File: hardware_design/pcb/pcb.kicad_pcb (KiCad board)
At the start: 2 copper layers, 117.2 x 110 mm, 98 parts, among them J1 Eurorack Power, J10 Conn_01x10_Socket, J11 Conn_01x10_Socket, J12 Conn_01x10_Pin, J13 Conn_01x10_Socket, J14 Conn_01x10_Pin, J15 Conn_01x10_Socket, J16 Conn_01x10_Pin, J2 Thonkiconn, J3 Thonkiconn, J4 Thonkiconn, J5 Thonkiconn, J6 Thonkiconn, J7 Thonkiconn, J9 Conn_01x10_Pin, Q1 DMG2305UX, Q2 MMBT3904, Q3 MMBT3904, SW1 SW_Rotary_1x4, SW2 SW_SPST, SW3 RotaryEncoder_Switch, SW4 SW_SPST, SW5 SW_Rotary_1x8, U1 Pico, U2 PCM1808, U3 TL072CD, U4 TL072CD, U5 GY_PCM5102A, U6 APS6404L, U7 LM1117MP-5.0, U8 MC14532B

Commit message: Rev 2 schematic & circuit board
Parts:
- removed C18, C19: 22u, Capacitor_SMD_AKL:CP_Elec_6.3x5.8
- removed C20: 100n, Capacitor_SMD_AKL:C_0603_1608Metric
- removed D3, D4, D5, D6: 1N4148WS, Diode_SMD_AKL:D_SOD-323
- removed the G*** at (123.7, 103.7)
- removed the G*** at (59.0, 34.3)
- removed the G*** at (59.7, 34.3)
- removed the G*** at (117.8, 81.4)
- removed R20: 4k7, Resistor_SMD_AKL:R_0603_1608Metric_Pad1.05x0.95mm_HandSolder
- removed R21: 3k3, Resistor_SMD_AKL:R_0603_1608Metric_Pad1.05x0.95mm_HandSolder
- removed R22: 10k, Resistor_SMD_AKL:R_0603_1608Metric_Pad1.05x0.95mm_HandSolder
- removed the REF** at (138.6, 36.4)
- removed the REF** at (59.2, 43.5) (x2)
- removed the REF** at (118.1, 89.9)
- added G***: LOGO, europi:AM_Logo, F.Cu at (117.0, 66.5)
- added G***: LOGO, europi:AM_Logo, F.Cu at (59.7, 35.8)
- added G***: LOGO, europi:AM_Logo, B.Cu at (58.1, 35.5)
- added G***: LOGO, europi:AM_Logo, B.Cu at (117.9, 66.4)
- added Q4: MMBT3906, Package_TO_SOT_SMD_AKL:SOT-23, B.Cu at (111.5, 85.0)
- added R31: 4k7, Resistor_SMD_AKL:R_0603_1608Metric_Pad1.05x0.95mm_HandSolder, B.Cu at (39.0, 70.8)
- added R32: 4k7, Resistor_SMD_AKL:R_0603_1608Metric_Pad1.05x0.95mm_HandSolder, B.Cu at (39.0, 73.8)
- added R33: 4k7, Resistor_SMD_AKL:R_0603_1608Metric_Pad1.05x0.95mm_HandSolder, B.Cu at (39.0, 76.8)
- added R34: 4k7, Resistor_SMD_AKL:R_0603_1608Metric_Pad1.05x0.95mm_HandSolder, B.Cu at (39.0, 79.8)
- added R35: 4k7, Resistor_SMD_AKL:R_0603_1608Metric_Pad1.05x0.95mm_HandSolder, B.Cu at (49.5, 79.8)
- added R36: 4k7, Resistor_SMD_AKL:R_0603_1608Metric_Pad1.05x0.95mm_HandSolder, B.Cu at (49.5, 76.8)
- added R37: 4k7, Resistor_SMD_AKL:R_0603_1608Metric_Pad1.05x0.95mm_HandSolder, B.Cu at (49.6, 73.8)
- added R38: 4k7, Resistor_SMD_AKL:R_0603_1608Metric_Pad1.05x0.95mm_HandSolder, B.Cu at (49.6, 70.8)
- added R39: 1k, Resistor_SMD_AKL:R_0603_1608Metric_Pad1.05x0.95mm_HandSolder, B.Cu at (128.1, 82.3)
- added R40: 1k, Resistor_SMD_AKL:R_0603_1608Metric_Pad1.05x0.95mm_HandSolder, B.Cu at (122.9, 80.0)
- added R41: 10k, Resistor_SMD_AKL:R_0603_1608Metric_Pad1.05x0.95mm_HandSolder, B.Cu at (111.6, 89.7)
- added R42: 100k, Resistor_SMD_AKL:R_0603_1608Metric_Pad1.05x0.95mm_HandSolder, B.Cu at (111.5, 80.0)
- added REF**: OSHW-Logo2_7.3x6mm_SilkScreen, Symbol:OSHW-Logo2_7.3x6mm_SilkScreen, F.Cu at (132.3, 66.6)
- added REF**: OSHW-Logo2_7.3x6mm_SilkScreen, Symbol:OSHW-Logo2_7.3x6mm_SilkScreen, F.Cu at (59.4, 43.8)
- added REF**: OSHW-Logo2_7.3x6mm_SilkScreen, Symbol:OSHW-Logo2_7.3x6mm_SilkScreen, B.Cu at (59.4, 43.7)
- added REF**: OSHW-Logo2_7.3x6mm_SilkScreen, Symbol:OSHW-Logo2_7.3x6mm_SilkScreen, B.Cu at (104.3, 66.3)
- added U9: MC14532B, Package_SO:SOIC-16_3.9x9.9mm_P1.27mm, B.Cu at (43.0, 55.0)
- C1, C2: value CP_SMD_D6.3mm_H5.8mm -> 47u; moved to F.Cu
- C3, Q2, Q3, R18, R19, U6: moved to B.Cu
- R1: moved to F.Cu
- SW1: value SW_Rotary_1x4 -> SW_Rotary_1x8
- U7: value LM1117MP-5.0 -> L7805; footprint Package_TO_SOT_SMD:SOT-223-3_TabPin2 -> Package_TO_SOT_SMD:TO-252-2
- moved Q3 49.2 mm to (122.8, 85.0), turned to 90 degrees
- moved R1 47.7 mm to (83.6, 99.5)
- moved R3 38.9 mm to (99.5, 43.6), turned to 0 degrees
- moved R5 38.5 mm to (99.5, 46.6)
- moved C3 28.2 mm to (128.1, 87.9), turned to 180 degrees
- moved C1 26.8 mm to (140.8, 103.6), turned to 180 degrees
- moved U8 26.3 mm to (75.6, 55.0), turned to 0 degrees
- moved R19 25.1 mm to (117.1, 89.8), turned to 0 degrees
- moved C7 25.0 mm to (137.9, 50.0)
- moved C6 19.8 mm to (137.9, 46.5)
- moved Q2 19.7 mm to (117.0, 85.0), turned to 90 degrees
- moved U6 19.0 mm to (133.6, 85.4), turned to -90 degrees
- moved R16 16.6 mm to (124.9, 50.7), turned to 0 degrees
- moved R8 16.3 mm to (99.5, 37.6)
- moved R18 15.8 mm to (117.1, 80.0)
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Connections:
- J11 pad 10: ALG_B -> ALG_C
- J11 pad 8: +3.3V -> ALG_A
- J11 pad 9: ALG_A -> ALG_B
- J12 pad 8: +3.3V -> B_8
- J15 pad 7: LED -> CLOCK_OUT
- J15 pad 8: +3.3V -> unconnected-(J15-Pin_8-Pad8)
- J16 pad 8: +3.3V -> unconnected-(J16-Pin_8-Pad8)
- Q3 pad 3: CLOCK_OUT_1 -> Net-(Q3-C)
- RV2 pad 1: P_5 -> P_9
- RV2 pad 3: P_9 -> P_5
- RV3 pad 1: P_5 -> P_9
- RV3 pad 3: P_9 -> P_5
- RV4 pad 1: P_5 -> P_9
- RV4 pad 3: P_9 -> P_5
- SW1 pad 2: unconnected-(SW1-Pad2) -> D9
- SW1 pad 3: Net-(D3-A) -> D10
- SW1 pad 4: Net-(D4-A) -> D11
- SW1 pad 5: Net-(D5-A) -> D12
- SW1 pad 6: unconnected-(SW1-Pad6) -> D13
- SW1 pad 7: unconnected-(SW1-Pad7) -> D14
- SW1 pad 8: unconnected-(SW1-Pad8) -> D15
- SW1 pad 9: unconnected-(SW1-Pad9) -> D16
- SW2 pad 1: +3.3V -> GND
- U1 pad 10: LED -> I2S_DOUT
- U1 pad 11: I2S_BCK -> I2S_DIN
- U1 pad 12: I2S_LRCK -> I2S_BCK
- U1 pad 14: I2S_SCK -> I2S_LRCK
- U1 pad 15: I2S_DIN -> I2S_SCK
- U1 pad 4: DIV_A -> ALG_C
- U1 pad 5: DIV_B -> DIV_A
- U1 pad 6: DIV_C -> DIV_B
- U1 pad 7: DIV_D -> DIV_C
- U1 pad 9: I2S_DOUT -> DIV_D
- U7 pad 1: GND -> VCC
- U7 pad 2: +5V -> GND
- U7 pad 3: VCC -> +5V
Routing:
- net GND: track 728.4 -> 893.3 mm, vias 0 -> 5
- net B_8: track 0.00 -> 94.2 mm, vias 0 -> 1
- net LED: track 54.2 -> 0.00 mm
- net B_9: track 52.1 -> 102.1 mm, vias 0 -> 1
- net E_7: track 3.15 -> 52.9 mm, vias 0 -> 1
- net ALG_C: track 0.00 -> 46.0 mm
- net B_2: track 37.6 -> 82.0 mm
- net B_10: track 61.5 -> 104.4 mm, vias 0 -> 2
- net LVOL_1: track 6.91 -> 45.5 mm, vias 0 -> 1
- net CLOCK_OUT_1: track 23.8 -> 60.4 mm
- net D11: track 0.00 -> 34.7 mm, vias 0 -> 1
- net D12: track 0.00 -> 33.8 mm, vias 0 -> 1
- net +3.3V: track 334.7 -> 300.9 mm, vias 1 -> 6
- net LIN_1: track 74.7 -> 106.3 mm, vias 0 -> 1
- net D15: track 0.00 -> 30.6 mm, vias 0 -> 1
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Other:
- board text added: "Camberwell Parrot Rev 2"
- board text removed: "+12v"
- board text removed: "Eurorack Power -12v (Red Stripe)"
- board text removed: "Parrot Rev 1"
- board text removed: "Raspberry Pi Pico"

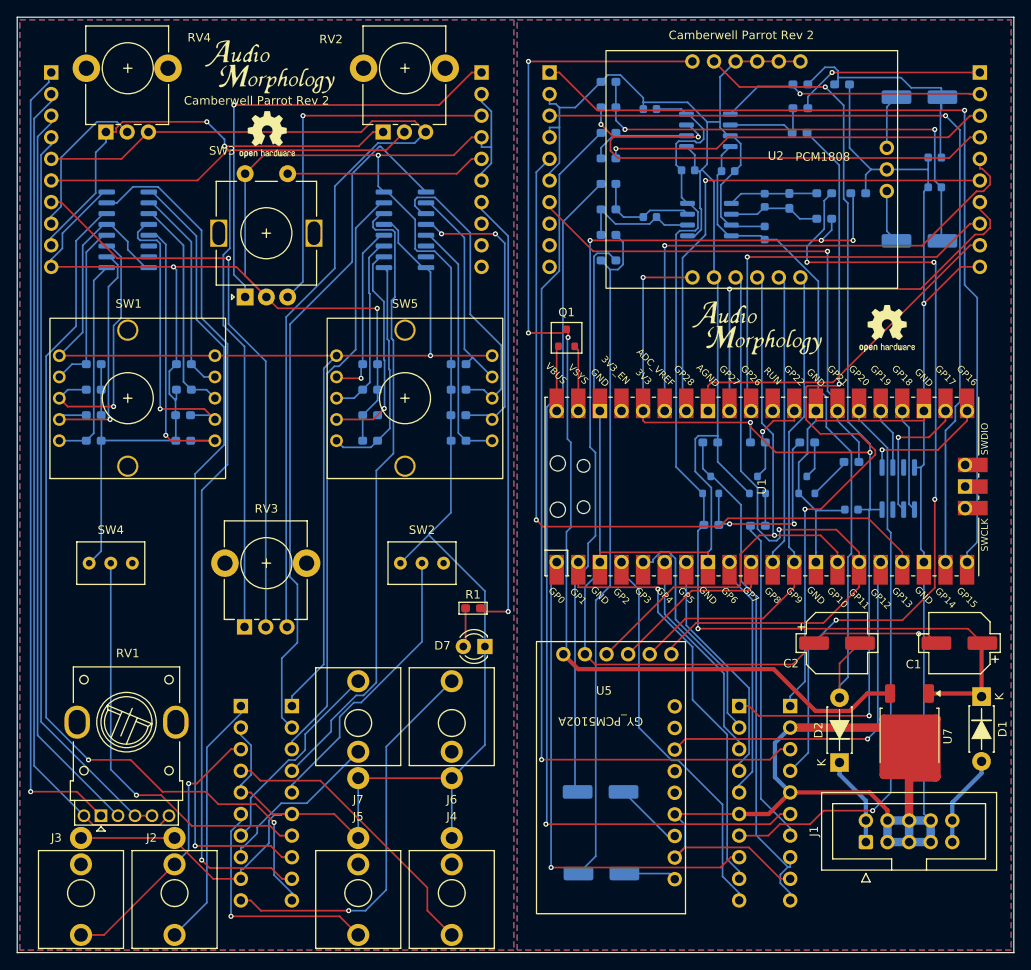
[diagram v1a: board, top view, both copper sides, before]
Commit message: Software switch de-bounce added as a result of Rev 2 testing.
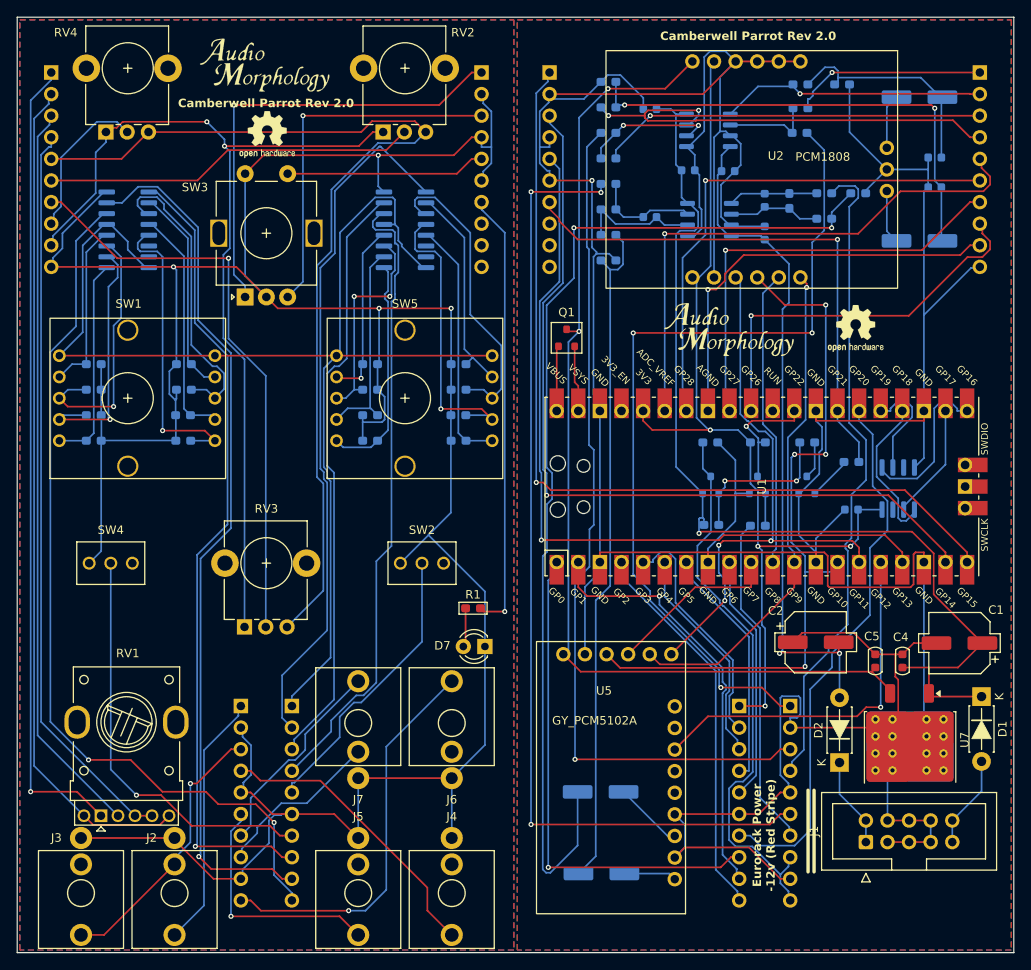
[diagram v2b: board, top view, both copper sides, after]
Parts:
- removed the G*** at (117.0, 66.5)
- removed the G*** at (59.7, 35.8)
- removed the G*** at (58.1, 35.5)
- removed the G*** at (117.9, 66.4)
- removed the REF** at (132.3, 66.6)
- removed the REF** at (59.4, 43.8)
- removed the REF** at (59.4, 43.7)
- removed the REF** at (104.3, 66.3)
- added C4: 300n, Capacitor_SMD_AKL:C_0603_1608Metric, F.Cu at (134.1, 105.7)
- added C5: 100n, Capacitor_SMD_AKL:C_0603_1608Metric, F.Cu at (130.9, 105.7)
- added G***: LOGO, europi:AM_Logo, F.Cu at (113.7, 66.7)
- added G***: LOGO, europi:AM_Logo, F.Cu at (59.1, 35.6)
- added G***: LOGO, europi:AM_Logo, B.Cu at (59.1, 35.6)
- added G***: LOGO, europi:AM_Logo, B.Cu at (124.2, 66.5)
- added REF**: OSHW-Logo2_7.3x6mm_SilkScreen, Symbol:OSHW-Logo2_7.3x6mm_SilkScreen, F.Cu at (59.4, 43.8)
- added REF**: OSHW-Logo2_7.3x6mm_SilkScreen, Symbol:OSHW-Logo2_7.3x6mm_SilkScreen, F.Cu at (128.6, 66.6)
- added REF**: OSHW-Logo2_7.3x6mm_SilkScreen, Symbol:OSHW-Logo2_7.3x6mm_SilkScreen, B.Cu at (109.3, 66.4)
- added REF**: OSHW-Logo2_7.3x6mm_SilkScreen, Symbol:OSHW-Logo2_7.3x6mm_SilkScreen, B.Cu at (59.4, 43.8)
- U7: footprint Package_TO_SOT_SMD:TO-252-2 -> DSP_CodecBoards:TO-252-2 with heatsink
- moved C2 2.50 mm to (123.9, 103.5)
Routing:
- net +3.3V: track 300.9 -> 268.2 mm, vias 6 -> 4
- net Net-(C10-Pad2): track 105.9 -> 124.7 mm, vias 3 -> 2
- net ROUT_1: track 95.8 -> 77.2 mm, vias 4 -> 0
- net I2S_LRCK: track 68.2 -> 85.4 mm, vias 1 -> 4
- net RIN_1: track 83.9 -> 101.0 mm, vias 2 -> 3
- net +5V: track 137.5 -> 122.7 mm, vias 3 -> 2
- net D10: track 26.2 -> 35.7 mm
- net I2S_SCK: track 75.4 -> 67.9 mm, vias 1 -> 3
- net LOUT_1: track 107.2 -> 114.7 mm, vias 1 -> 3
- net LVOL_2: track 62.8 -> 55.5 mm
- net AGND: track 41.8 -> 48.9 mm, vias 0 -> 1
- net D11: track 34.7 -> 27.8 mm, vias 1 -> 0
- net CLOCK_OUT_1: track 60.4 -> 66.0 mm
- net SPI_MOSI: track 12.2 -> 17.7 mm
- net SPI_MISO: track 7.24 -> 12.7 mm
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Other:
- board text added: "Camberwell Parrot Rev 2.0"
- board text added: "Eurorack Power -12v (Red Stripe)"
- board text removed: "Camberwell Parrot Rev 2"

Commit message: Rev 2.1 hardware changes
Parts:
- removed G*** (x4): LOGO, europi:AM_Logo
- removed REF** (x4): OSHW-Logo2_7.3x6mm_SilkScreen, Symbol:OSHW-Logo2_7.3x6mm_SilkScreen
- moved R23 1.12 mm to (80.8, 70.8)
- moved R24 1.12 mm to (80.8, 73.8)
- moved R25 1.12 mm to (80.8, 76.8)
- moved R26 1.12 mm to (80.8, 79.8)
- moved R27 1.12 mm to (70.4, 79.8)
- moved R28 1.12 mm to (70.4, 76.8)
- moved R29 1.12 mm to (70.4, 73.8)
- moved R30 1.12 mm to (70.4, 70.8)
- moved R31 1.12 mm to (37.9, 70.8)
- moved R32 1.12 mm to (37.9, 73.8)
- moved R33 1.12 mm to (37.9, 76.8)
- moved R34 1.12 mm to (37.9, 79.8)
- moved R35 1.12 mm to (48.4, 79.8)
- moved R36 1.12 mm to (48.4, 76.8)
- moved R37 1.12 mm to (48.5, 73.8)
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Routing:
- net SYNC_FREE: track 64.0 -> 93.4 mm, vias 0 -> 3
- net ROUT_1: track 77.2 -> 99.3 mm, vias 0 -> 2
- net RIN_1: track 101.0 -> 78.9 mm, vias 3 -> 0
- net LOUT_1: track 114.7 -> 96.8 mm, vias 3 -> 2
- net GND: track 888.3 -> 873.2 mm, vias 5 -> 9
- net I2S_SCK: track 67.9 -> 82.7 mm, vias 3 -> 2
- net +3.3V: track 268.2 -> 282.6 mm
- net T_7: track 24.3 -> 34.9 mm, vias 0 -> 2
- net I2S_LRCK: track 85.4 -> 75.0 mm, vias 4 -> 1
- net D10: track 35.7 -> 25.7 mm
- net B_2: track 81.9 -> 72.2 mm, vias 0 -> 1
- net D1: track 35.6 -> 25.9 mm
- net Net-(Q4-B): track 18.6 -> 28.2 mm
- net CLOCK_IN: track 14.4 -> 23.7 mm
- net B_8: track 94.8 -> 86.6 mm, vias 1 -> 0
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- removed copper zone on B.Cu, net GND
- removed copper zone on F.Cu, net GND
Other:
- board text added: "Camberwell Parrot Rev 2.1"
- board text removed: "Camberwell Parrot Rev 2.0"
